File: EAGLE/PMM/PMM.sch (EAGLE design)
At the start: 19 parts, among them J1 TB001-500-12BE, K1 EC2-5NU, K2 G6DN-1A_DC5, K3 35701331, K4 35701331

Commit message: Minor format fixes
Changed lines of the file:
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@@
 <attribute name="VALUE" x="26.67" y="56.134" size="1.27" layer="96"/>
 </instance>
-<instance part="GND1" gate="1" x="123.19" y="93.98" smashed="yes">
-<attribute name="VALUE" x="120.65" y="91.44" size="1.778" layer="96"/>
+<instance part="GND1" gate="1" x="69.85" y="101.6" smashed="yes">
+<attribute name="VALUE" x="67.31" y="99.06" size="1.778" layer="96"/>
 </instance>
 <instance part="GND2" gate="1" x="-81.28" y="11.43" smashed="yes">
@@
 <pinref part="K2" gate="A" pin="2"/>
 <pinref part="GND1" gate="1" pin="GND"/>
-<wire x1="63.5" y1="110.49" x2="123.19" y2="110.49" width="0.1524" layer="91"/>
-<wire x1="123.19" y1="110.49" x2="123.19" y2="96.52" width="0.1524" layer="91"/>
+<wire x1="63.5" y1="110.49" x2="69.85" y2="110.49" width="0.1524" layer="91"/>
+<wire x1="69.85" y1="110.49" x2="69.85" y2="104.14" width="0.1524" layer="91"/>
 </segment>
 <segment>

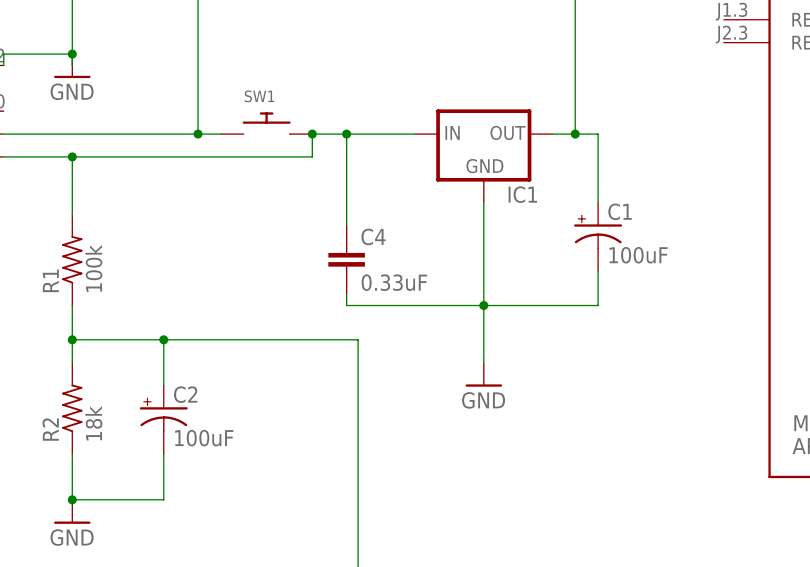
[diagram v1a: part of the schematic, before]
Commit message: Updated C4 value
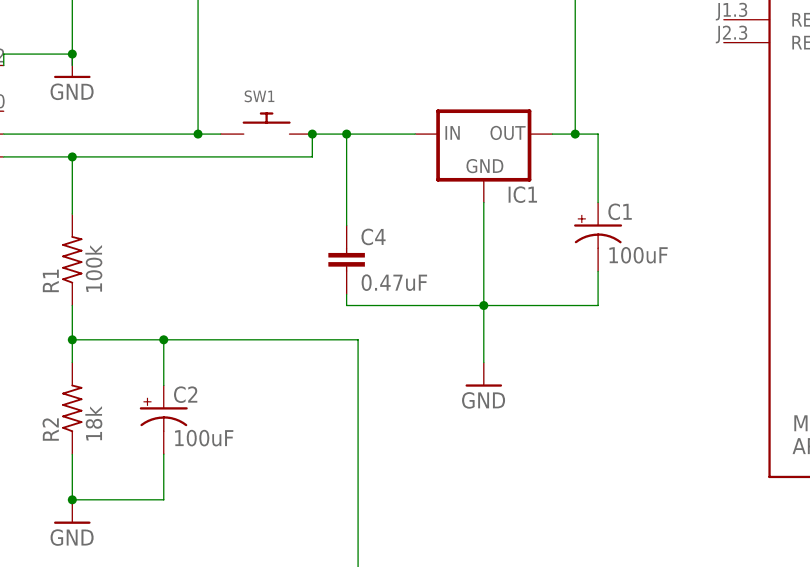
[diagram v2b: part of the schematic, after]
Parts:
- C4: value 0.33uF -> 0.47uF
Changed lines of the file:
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@@
 <part name="C2" library="adafruit" library_urn="urn:adsk.eagle:library:420" deviceset="CPOL-US" device="E2.5-7" package3d_urn="urn:adsk.eagle:package:6240501/1" value="100uF"/>
 <part name="C3" library="adafruit" library_urn="urn:adsk.eagle:library:420" deviceset="CPOL-US" device="E2.5-7" package3d_urn="urn:adsk.eagle:package:6240501/1" value="100uF"/>
-<part name="C4" library="capacitor-wima" library_urn="urn:adsk.eagle:library:116" deviceset="C" device="10/6" package3d_urn="urn:adsk.eagle:package:5401/1" value="0.33uF"/>
+<part name="C4" library="capacitor-wima" library_urn="urn:adsk.eagle:library:116" deviceset="C" device="10/6" package3d_urn="urn:adsk.eagle:package:5401/1" value="0.47uF"/>
 <part name="J1" library="TB001-500-12BE" deviceset="TB001-500-12BE" device=""/>
 <part name="K3" library="relay" library_urn="urn:adsk.eagle:library:339" deviceset="35701331" device="" package3d_urn="urn:adsk.eagle:package:24297/1"/>

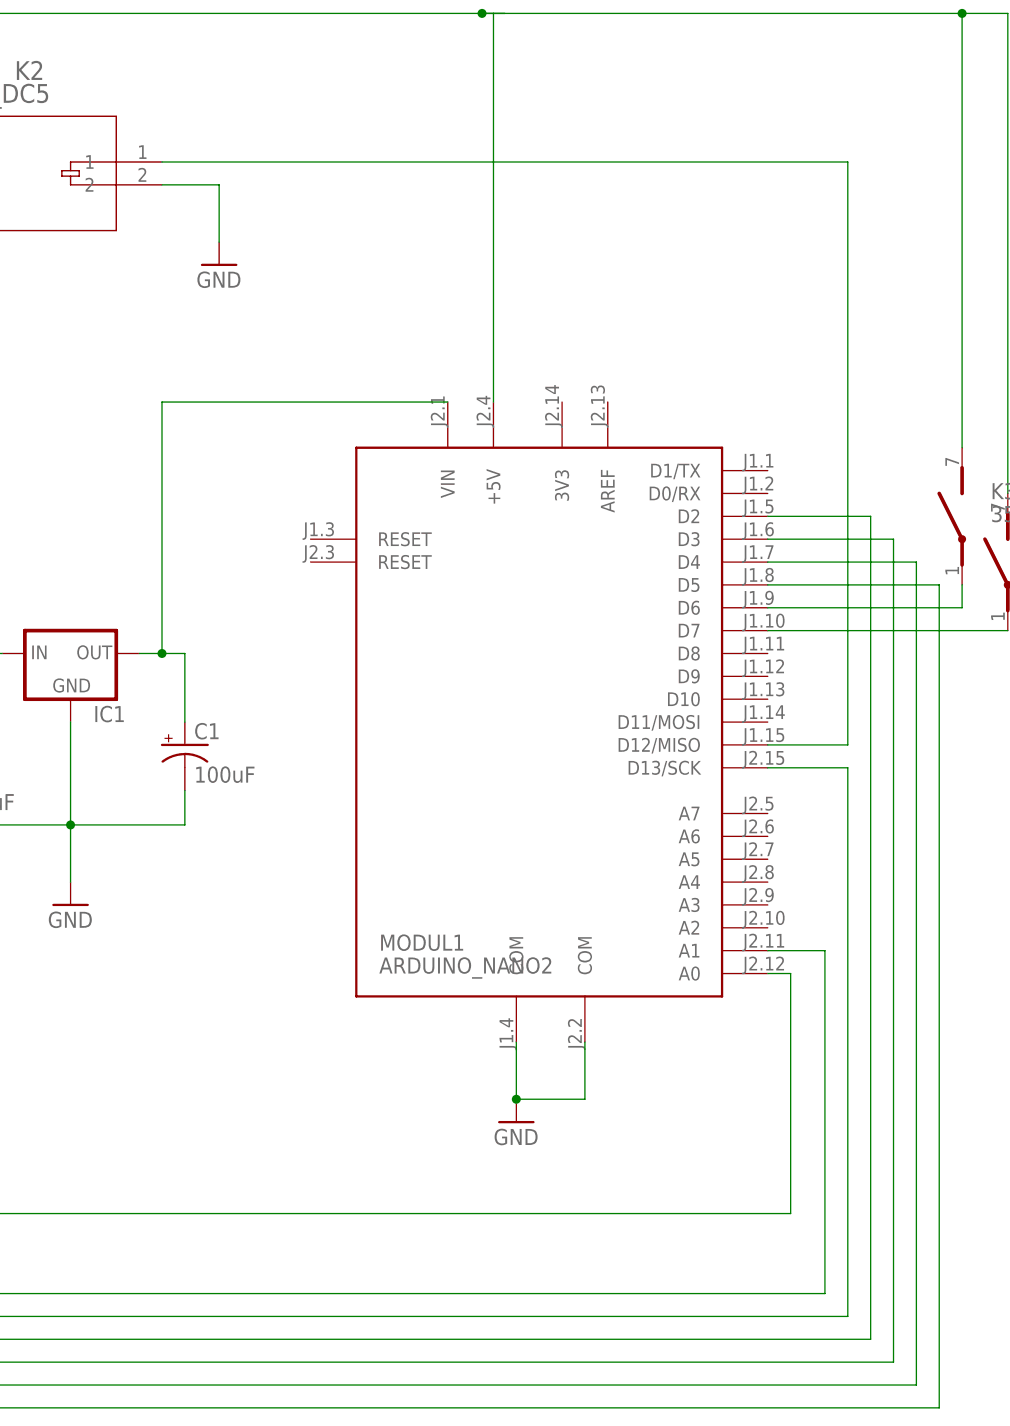
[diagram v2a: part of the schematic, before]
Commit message: Switched D12 & D13 to have on-board indicator for on state
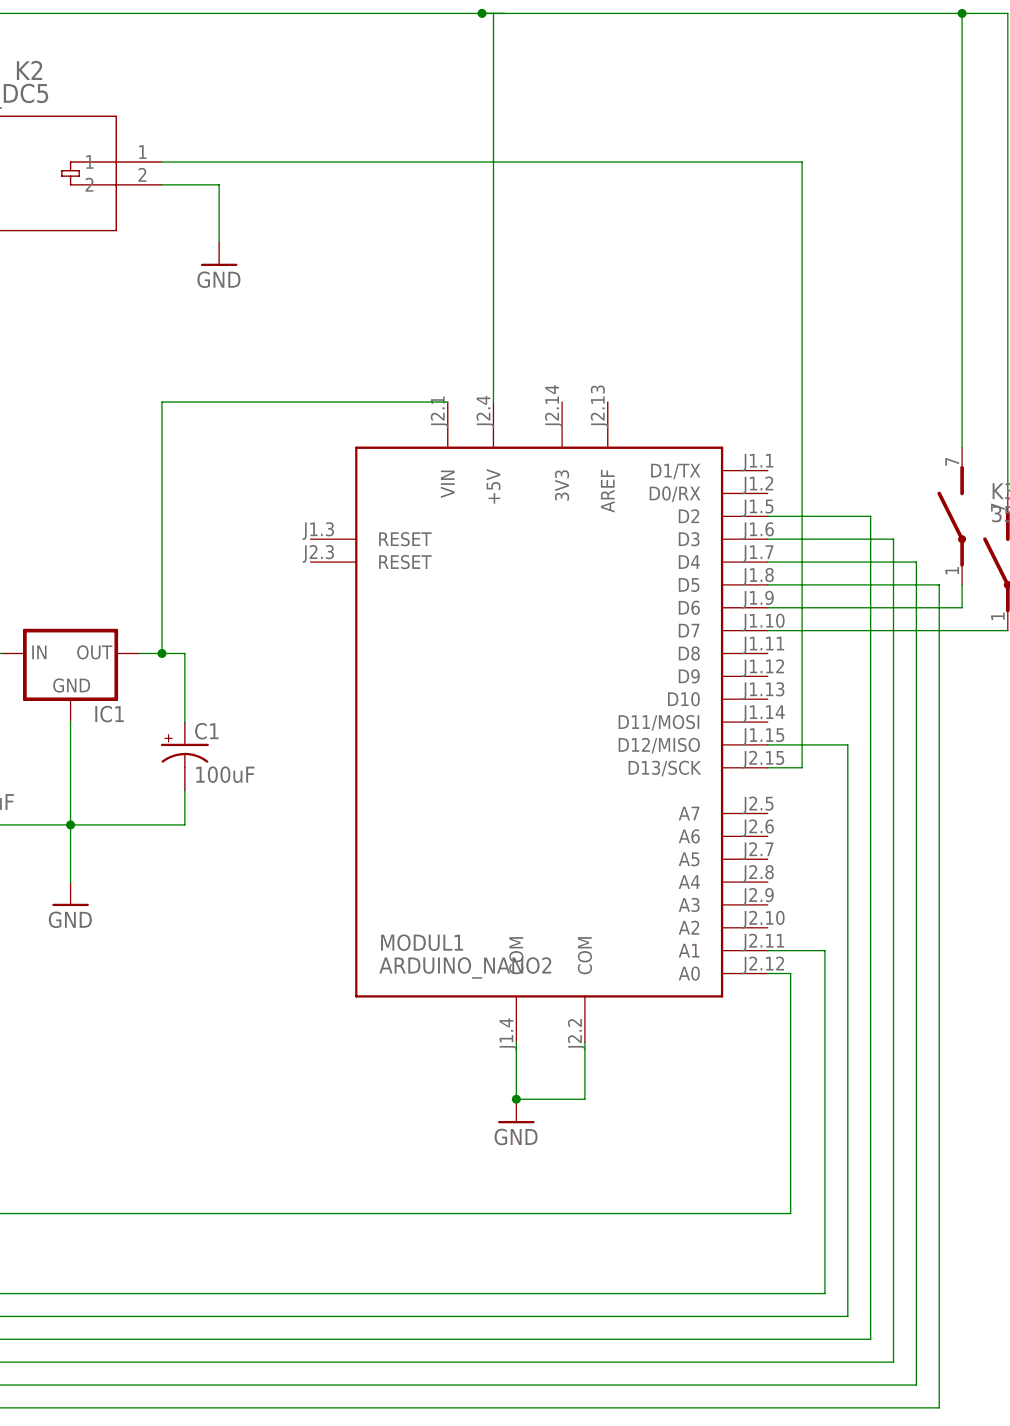
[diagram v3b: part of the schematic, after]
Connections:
- removed net N$6: K1.1, MODUL1.D13/SCK
- new net N$22: K1.1, MODUL1.D12/MISO
- net N$5: now also MODUL1.D13/SCK; no longer MODUL1.D12/MISO
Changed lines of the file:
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@@
-</segment>
-</net>
-<net name="N$5" class="0">
-<segment>
-<pinref part="MODUL1" gate="MODUL" pin="D12/MISO"/>
-<wire x1="130.81" y1="48.26" x2="139.7" y2="48.26" width="0.1524" layer="91"/>
-<wire x1="139.7" y1="48.26" x2="139.7" y2="113.03" width="0.1524" layer="91"/>
-<pinref part="K2" gate="A" pin="1"/>
-<wire x1="139.7" y1="113.03" x2="63.5" y2="113.03" width="0.1524" layer="91"/>
-</segment>
-</net>
-<net name="N$6" class="0">
-<segment>
-<pinref part="MODUL1" gate="MODUL" pin="D13/SCK"/>
-<wire x1="130.81" y1="45.72" x2="139.7" y2="45.72" width="0.1524" layer="91"/>
-<wire x1="139.7" y1="45.72" x2="139.7" y2="-15.24" width="0.1524" layer="91"/>
-<wire x1="139.7" y1="-15.24" x2="-57.15" y2="-15.24" width="0.1524" layer="91"/>
-<pinref part="K1" gate="G$1" pin="1"/>
-<wire x1="-57.15" y1="-15.24" x2="-57.15" y2="66.04" width="0.1524" layer="91"/>
-<wire x1="-57.15" y1="66.04" x2="-15.24" y2="66.04" width="0.1524" layer="91"/>
 </segment>
 </net>
@@
 </segment>
 </net>
+<net name="N$22" class="0">
+<segment>
+<pinref part="MODUL1" gate="MODUL" pin="D12/MISO"/>
+<wire x1="130.81" y1="48.26" x2="139.7" y2="48.26" width="0.1524" layer="91"/>
+<wire x1="139.7" y1="48.26" x2="139.7" y2="-15.24" width="0.1524" layer="91"/>
+<wire x1="139.7" y1="-15.24" x2="-57.15" y2="-15.24" width="0.1524" layer="91"/>
+<pinref part="K1" gate="G$1" pin="1"/>
+<wire x1="-57.15" y1="-15.24" x2="-57.15" y2="66.04" width="0.1524" layer="91"/>
+<wire x1="-57.15" y1="66.04" x2="-15.24" y2="66.04" width="0.1524" layer="91"/>
+</segment>
+</net>
+<net name="N$5" class="0">
+<segment>
+<pinref part="MODUL1" gate="MODUL" pin="D13/SCK"/>
+<wire x1="130.81" y1="45.72" x2="134.62" y2="45.72" width="0.1524" layer="91"/>
+<pinref part="K2" gate="A" pin="1"/>
+<wire x1="134.62" y1="45.72" x2="134.62" y2="113.03" width="0.1524" layer="91"/>
+<wire x1="134.62" y1="113.03" x2="63.5" y2="113.03" width="0.1524" layer="91"/>
+</segment>
+</net>

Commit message: Corrected SW2 footprint
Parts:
- SW2: device JWM:M20130 -> JWM:M20130M2013S2A2W30
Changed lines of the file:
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@@
 <grid distance="0.1" unitdist="inch" unit="inch" style="lines" multiple="1" display="no" altdistance="0.01" altunitdist="inch" altunit="inch"/>
 <layers>
-<layer number="1" name="Top" color="4" fill="1" visible="no" active="no"/>
-<layer number="2" name="Route2" color="1" fill="3" visible="no" active="no"/>
-<layer number="15" name="Route15" color="4" fill="6" visible="no" active="no"/>
-<layer number="16" name="Bottom" color="1" fill="1" visible="no" active="no"/>
-<layer number="17" name="Pads" color="2" fill="1" visible="no" active="no"/>
-<layer number="18" name="Vias" color="2" fill="1" visible="no" active="no"/>
-<layer number="19" name="Unrouted" color="6" fill="1" visible="no" active="no"/>
-<layer number="20" name="Dimension" color="15" fill="1" visible="no" active="no"/>
-<layer number="21" name="tPlace" color="7" fill="1" visible="no" active="no"/>
-<layer number="22" name="bPlace" color="7" fill="1" visible="no" active="no"/>
-<layer number="23" name="tOrigins" color="15" fill="1" visible="no" active="no"/>
-<layer number="24" name="bOrigins" color="15" fill="1" visible="no" active="no"/>
-<layer number="25" name="tNames" color="7" fill="1" visible="no" active="no"/>
-<layer number="26" name="bNames" color="7" fill="1" visible="no" active="no"/>
-<layer number="27" name="tValues" color="7" fill="1" visible="no" active="no"/>
-<layer number="28" name="bValues" color="7" fill="1" visible="no" active="no"/>
+<layer number="1" name="Top" color="4" fill="1" visible="yes" active="no"/>
+<layer number="2" name="Route2" color="16" fill="1" visible="yes" active="no"/>
+<layer number="15" name="Route15" color="23" fill="1" visible="yes" active="no"/>
+<layer number="16" name="Bottom" color="1" fill="1" visible="yes" active="no"/>
+<layer number="17" name="Pads" color="2" fill="1" visible="yes" active="no"/>
+<layer number="18" name="Vias" color="2" fill="1" visible="yes" active="no"/>
+<layer number="19" name="Unrouted" color="6" fill="1" visible="yes" active="no"/>
+<layer number="20" name="Dimension" color="24" fill="1" visible="yes" active="no"/>
+<layer number="21" name="tPlace" color="7" fill="1" visible="yes" active="no"/>
+<layer number="22" name="bPlace" color="7" fill="1" visible="yes" active="no"/>
+<layer number="23" name="tOrigins" color="15" fill="1" visible="yes" active="no"/>
+<layer number="24" name="bOrigins" color="15" fill="1" visible="yes" active="no"/>
+<layer number="25" name="tNames" color="7" fill="1" visible="yes" active="no"/>
+<layer number="26" name="bNames" color="7" fill="1" visible="yes" active="no"/>
+<layer number="27" name="tValues" color="7" fill="1" visible="yes" active="no"/>
+<layer number="28" name="bValues" color="7" fill="1" visible="yes" active="no"/>
 <layer number="29" name="tStop" color="7" fill="3" visible="no" active="no"/>
 <layer number="30" name="bStop" color="7" fill="6" visible="no" active="no"/>
@@
 <layer number="35" name="tGlue" color="7" fill="4" visible="no" active="no"/>
 <layer number="36" name="bGlue" color="7" fill="5" visible="no" active="no"/>
-<layer number="37" name="tTest" color="7" fill="1" visible="no" active="no"/>
-<layer number="38" name="bTest" color="7" fill="1" visible="no" active="no"/>
+<layer number="37" name="tTest" color="7" fill="1" visible="yes" active="no"/>
+<layer number="38" name="bTest" color="7" fill="1" visible="yes" active="no"/>
 <layer number="39" name="tKeepout" color="4" fill="11" visible="no" active="no"/>
 <layer number="40" name="bKeepout" color="1" fill="11" visible="no" active="no"/>
@@
 <layer number="44" name="Drills" color="7" fill="1" visible="no" active="no"/>
 <layer number="45" name="Holes" color="7" fill="1" visible="no" active="no"/>
-<layer number="46" name="Milling" color="3" fill="1" visible="no" active="no"/>
-<layer number="47" name="Measures" color="7" fill="1" visible="no" active="no"/>
-<layer number="48" name="Document" color="7" fill="1" visible="no" active="no"/>
-<layer number="49" name="Reference" color="7" fill="1" visible="no" active="no"/>
-<layer number="50" name="dxf" color="7" fill="1" visible="no" active="no"/>
-<layer number="51" name="tDocu" color="7" fill="1" visible="no" active="no"/>
-<layer number="52" name="bDocu" color="7" fill="1" visible="no" active="no"/>
-<layer number="53" name="tGND_GNDA" color="7" fill="9" visible="no" active="no"/>
-<layer number="54" name="bGND_GNDA" color="1" fill="9" visible="no" active="no"/>
-<layer number="56" name="wert" color="7" fill="1" visible="no" active="no"/>
-<layer number="57" name="tCAD" color="7" fill="1" visible="no" active="no"/>
-<layer number="59" name="tCarbon" color="7" fill="1" visible="no" active="no"/>
-<layer number="60" name="bCarbon" color="7" fill="1" visible="no" active="no"/>
+<layer number="46" name="Milling" color="3" fill="1" visible="yes" active="no"/>
+<layer number="47" name="Measures" color="7" fill="1" visible="yes" active="no"/>
+<layer number="48" name="Document" color="7" fill="1" visible="yes" active="no"/>
+<layer number="49" name="Reference" color="7" fill="1" visible="yes" active="no"/>
+<layer number="50" name="dxf" color="7" fill="1" visible="yes" active="no"/>
+<layer number="51" name="tDocu" color="7" fill="1" visible="yes" active="no"/>
+<layer number="52" name="bDocu" color="7" fill="1" visible="yes" active="no"/>
+<layer number="53" name="tGND_GNDA" color="7" fill="9" visible="yes" active="no"/>
+<layer number="54" name="bGND_GNDA" color="1" fill="9" visible="yes" active="no"/>
+<layer number="56" name="wert" color="7" fill="1" visible="yes" active="no"/>
+<layer number="57" name="tCAD" color="7" fill="1" visible="yes" active="no"/>
+<layer number="59" name="tCarbon" color="7" fill="1" visible="yes" active="no"/>
+<layer number="60" name="bCarbon" color="7" fill="1" visible="yes" active="no"/>
 <layer number="88" name="SimResults" color="9" fill="1" visible="yes" active="yes"/>
 <layer number="89" name="SimProbes" color="9" fill="1" visible="yes" active="yes"/>
@@
 <part name="K1" library="EC2-5NU" deviceset="EC2-5NU" device=""/>
 <part name="K2" library="G6DN" deviceset="G6DN-1A_DC5" device=""/>
-<part name="SW2" library="JWM" deviceset="M201*30" device="" package3d_urn="urn:adsk.eagle:package:27677/1"/>
+<part name="SW2" library="JWM" deviceset="M201*30" device="M2013S2A2W30" package3d_urn="urn:adsk.eagle:package:27677/1"/>
 <part name="SW1" library="JWM" deviceset="SWITCH_PUSHBUTTON" device="ON-MOM.2" package3d_urn="urn:adsk.eagle:package:6240957/1"/>
 <part name="GND1" library="supply1" library_urn="urn:adsk.eagle:library:371" deviceset="GND" device=""/>
